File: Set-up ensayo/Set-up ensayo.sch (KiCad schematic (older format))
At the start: 14 parts, among them J1 Conn_Coaxial, J2 DB9_Female_MountingHoles

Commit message: Agregué al esquemático un potenciómetro variable y su footprint en paralelo a R de ensayo en caso de que necesite ser variada
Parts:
- added RV1: R_POT, Footprints proyecto:Potentiometer_Vishay_248GJ-249GJ_Single_Vertical, symbol Device:R_POT
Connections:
- net VZs1: now also RV1.2, RV1.3
- net Vi: now also RV1.1
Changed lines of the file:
@@
 Connection ~ 6900 4350
 Wire Wire Line
-	5400 3400 5200 3400
+	5400 3400 5300 3400
 Wire Wire Line
 	5700 3400 5950 3400
@@
 Text Label 2400 3500 0    50   ~ 0
 VAC
+$Comp
+L Device:R_POT RV1
+U 1 1 5D5409ED
+P 5550 3750
+F 0 "RV1" V 5435 3750 50  0000 C CNN
+F 1 "R_POT" V 5344 3750 50  0000 C CNN
+F 2 "Footprints proyecto:Potentiometer_Vishay_248GJ-249GJ_Single_Vertical" H 5550 3750 50  0001 C CNN
+F 3 "~" H 5550 3750 50  0001 C CNN
+F 4 "Resistencia auxiliar variable" V 5550 3750 50  0001 C CNN "Función"
+	1    5550 3750
+	0    -1   -1   0
+$EndComp
+Wire Wire Line
+	5300 3400 5300 3750
+Wire Wire Line
+	5300 3750 5400 3750
+Connection ~ 5300 3400
+Wire Wire Line
+	5300 3400 5200 3400
+Wire Wire Line
+	5550 3600 5950 3600
+Wire Wire Line
+	5950 3600 5950 3400
+Wire Wire Line
+	5700 3750 5950 3750
+Wire Wire Line
+	5950 3750 5950 3600
+Connection ~ 5950 3600
 $EndSCHEMATC

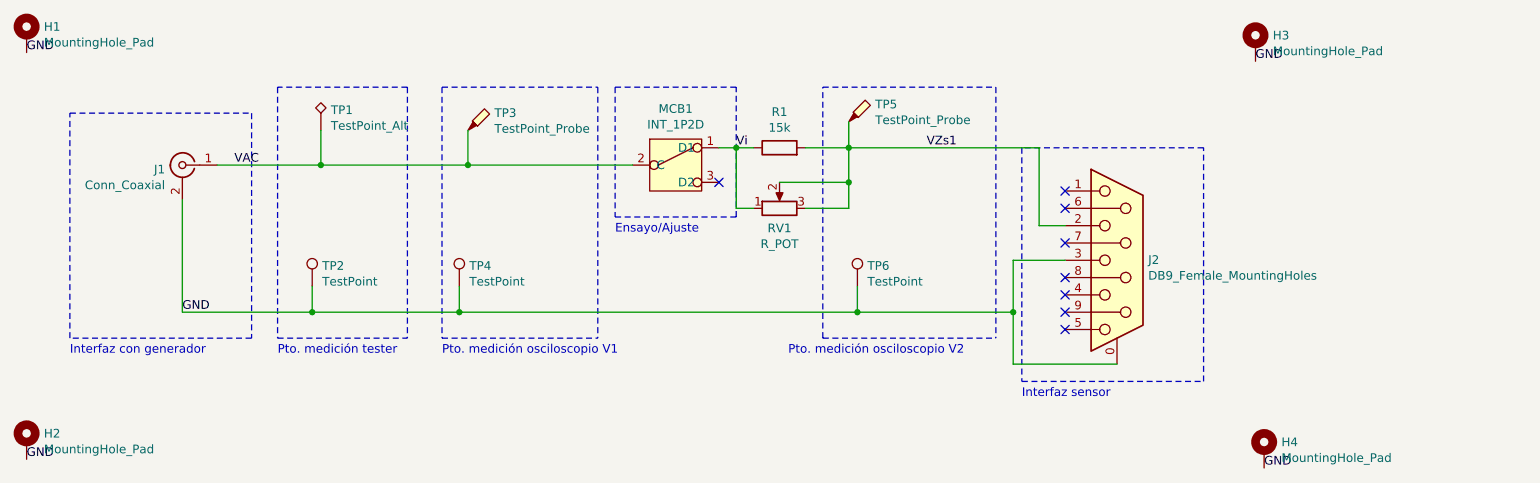
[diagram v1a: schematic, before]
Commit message: Agregué pines para configuración de resistencia variable o fija para ensayo
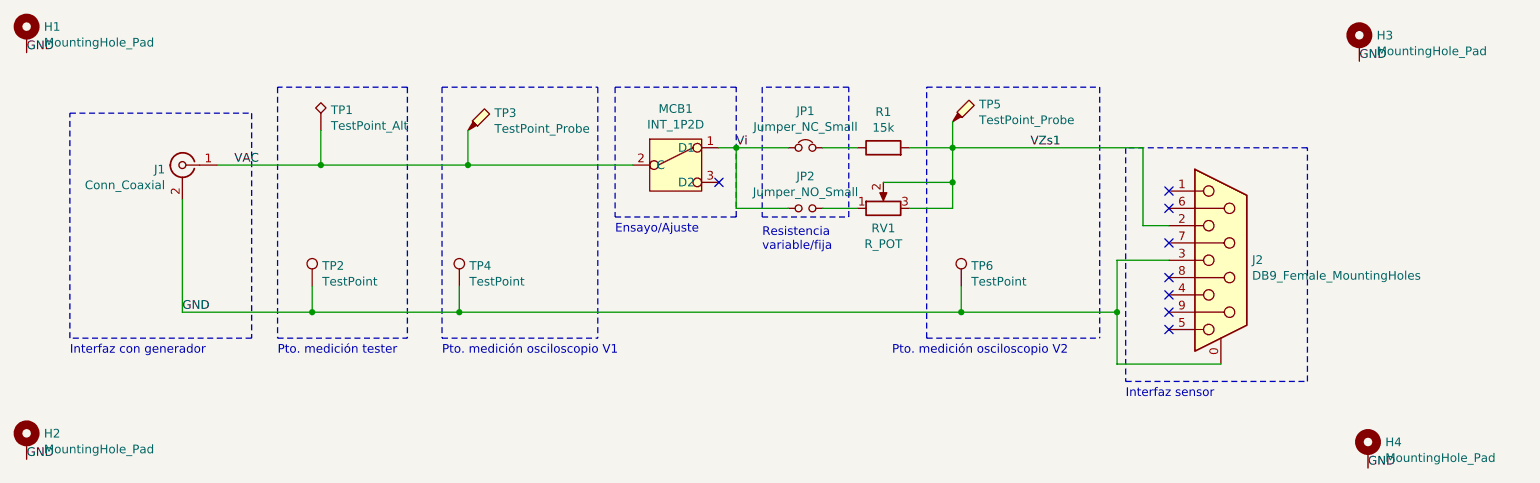
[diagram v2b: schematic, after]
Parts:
- added JP1: Jumper_NC_Small, Footprints proyecto:PinHeader_1x02_P1.00mm_Vertical, symbol Device:Jumper_NC_Small
- added JP2: Jumper_NO_Small, Footprints proyecto:PinHeader_1x02_P1.00mm_Vertical, symbol Device:Jumper_NO_Small
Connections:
- net Vi: now also JP1.1, JP2.1; no longer R1.1, RV1.1
- new net: JP1.2, R1.1
- new net: JP2.2, RV1.1
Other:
- note added: "Resistencia\nvariable/fija"
- moved on the sheet: H3, H4, J2, R1, RV1, TP5, TP6
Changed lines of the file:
@@
 L Mechanical:MountingHole_Pad H3
 U 1 1 5D42E2DA
-P 8300 2800
-F 0 "H3" H 8400 2849 50  0000 L CNN
-F 1 "MountingHole_Pad" H 8400 2758 50  0000 L CNN
-F 2 "Footprints proyecto:MountingHole_3.2mm_M3_ISO14580_Pad" H 8300 2800 50  0001 C CNN
-F 3 "~" H 8300 2800 50  0001 C CNN
-F 4 "Fijación e interfaz eléctrica con chasis" H 8300 2800 50  0001 C CNN "Función"
-	1    8300 2800
+P 8900 2800
+F 0 "H3" H 9000 2849 50  0000 L CNN
+F 1 "MountingHole_Pad" H 9000 2758 50  0000 L CNN
+F 2 "Footprints proyecto:MountingHole_3.2mm_M3_ISO14580_Pad" H 8900 2800 50  0001 C CNN
+F 3 "~" H 8900 2800 50  0001 C CNN
+F 4 "Fijación e interfaz eléctrica con chasis" H 8900 2800 50  0001 C CNN "Función"
+	1    8900 2800
 	1    0    0    -1
 $EndComp
@@
 L Mechanical:MountingHole_Pad H4
 U 1 1 5D42EA1B
-P 8350 5150
-F 0 "H4" H 8450 5199 50  0000 L CNN
-F 1 "MountingHole_Pad" H 8450 5108 50  0000 L CNN
-F 2 "Footprints proyecto:MountingHole_3.2mm_M3_ISO14580_Pad" H 8350 5150 50  0001 C CNN
-F 3 "~" H 8350 5150 50  0001 C CNN
-F 4 "Fijación e interfaz eléctrica con chasis" H 8350 5150 50  0001 C CNN "Función"
-	1    8350 5150
+P 8950 5150
+F 0 "H4" H 9050 5199 50  0000 L CNN
+F 1 "MountingHole_Pad" H 9050 5108 50  0000 L CNN
+F 2 "Footprints proyecto:MountingHole_3.2mm_M3_ISO14580_Pad" H 8950 5150 50  0001 C CNN
+F 3 "~" H 8950 5150 50  0001 C CNN
+F 4 "Fijación e interfaz eléctrica con chasis" H 8950 5150 50  0001 C CNN "Función"
+	1    8950 5150
 	1    0    0    -1
 $EndComp
@@
 L Device:R R1
 U 1 1 5D441970
-P 5550 3400
-F 0 "R1" V 5757 3400 50  0000 C CNN
-F 1 "15k" V 5666 3400 50  0000 C CNN
-F 2 "Footprints proyecto:R_Axial_DIN0204_L3.6mm_D1.6mm_P7.62mm_Horizontal" V 5480 3400 50  0001 C CNN
-F 3 "~" H 5550 3400 50  0001 C CNN
-F 4 "Resistencia de medición de sensor" V 5550 3400 50  0001 C CNN "Función"
-	1    5550 3400
+P 6150 3400
+F 0 "R1" V 6357 3400 50  0000 C CNN
+F 1 "15k" V 6266 3400 50  0000 C CNN
+F 2 "Footprints proyecto:R_Axial_DIN0204_L3.6mm_D1.6mm_P7.62mm_Horizontal" V 6080 3400 50  0001 C CNN
+F 3 "~" H 6150 3400 50  0001 C CNN
+F 4 "Resistencia de medición de sensor" V 6150 3400 50  0001 C CNN "Función"
+	1    6150 3400
 	0    -1   -1   0
 $EndComp
@@
 L Connector:DB9_Female_MountingHoles J2
 U 1 1 5D442DB3
-P 7500 4050
-F 0 "J2" H 7680 4052 50  0000 L CNN
-F 1 "DB9_Female_MountingHoles" H 7680 3961 50  0000 L CNN
-F 2 "Footprints proyecto:DSUB-9_Female_Horizontal_P2.77x2.84mm_EdgePinOffset4.94mm_Housed_MountingHolesOffset7.48mm" H 7500 4050 50  0001 C CNN
-F 3 " ~" H 7500 4050 50  0001 C CNN
-F 4 "Interfaz eléctrica con sensores" H 7500 4050 50  0001 C CNN "Función"
-	1    7500 4050
+P 8100 4050
+F 0 "J2" H 8280 4052 50  0000 L CNN
+F 1 "DB9_Female_MountingHoles" H 8280 3961 50  0000 L CNN
+F 2 "Footprints proyecto:DSUB-9_Female_Horizontal_P2.77x2.84mm_EdgePinOffset4.94mm_Housed_MountingHolesOffset7.48mm" H 8100 4050 50  0001 C CNN
+F 3 " ~" H 8100 4050 50  0001 C CNN
+F 4 "Interfaz eléctrica con sensores" H 8100 4050 50  0001 C CNN "Función"
+	1    8100 4050
 	1    0    0    -1
 $EndComp
@@
 L Connector:TestPoint_Probe TP5
 U 1 1 5D484196
-P 5950 3250
-F 0 "TP5" H 6103 3351 50  0000 L CNN
-F 1 "TestPoint_Probe" H 6103 3260 50  0000 L CNN
-F 2 "Footprints proyecto:PinHeader_1x01_P1.00mm_Horizontal" H 6150 3250 50  0001 C CNN
-F 3 "~" H 6150 3250 50  0001 C CNN
-F 4 "Interfaz eléctrica con punta de medición V2 osciloscopio" H 5950 3250 50  0001 C CNN "Función"
-	1    5950 3250
+P 6550 3250
+F 0 "TP5" H 6703 3351 50  0000 L CNN
+F 1 "TestPoint_Probe" H 6703 3260 50  0000 L CNN
+F 2 "Footprints proyecto:PinHeader_1x01_P1.00mm_Horizontal" H 6750 3250 50  0001 C CNN
+F 3 "~" H 6750 3250 50  0001 C CNN
+F 4 "Interfaz eléctrica con punta de medición V2 osciloscopio" H 6550 3250 50  0001 C CNN "Función"
+	1    6550 3250
 	1    0    0    -1
 $EndComp
@@
 L Connector:TestPoint TP6
 U 1 1 5D4852D2
-P 6000 4200
-F 0 "TP6" H 6058 4318 50  0000 L CNN
-F 1 "TestPoint" H 6058 4227 50  0000 L CNN
-F 2 "Footprints proyecto:PinHeader_1x01_P1.00mm_Horizontal" H 6200 4200 50  0001 C CNN
-F 3 "~" H 6200 4200 50  0001 C CNN
-F 4 "Interfaz eléctrica con GND de V2 osciloscopio" H 6000 4200 50  0001 C CNN "Función"
-	1    6000 4200
+P 6600 4200
+F 0 "TP6" H 6658 4318 50  0000 L CNN
+F 1 "TestPoint" H 6658 4227 50  0000 L CNN
+F 2 "Footprints proyecto:PinHeader_1x01_P1.00mm_Horizontal" H 6800 4200 50  0001 C CNN
+F 3 "~" H 6800 4200 50  0001 C CNN
+F 4 "Interfaz eléctrica con GND de V2 osciloscopio" H 6600 4200 50  0001 C CNN "Función"
+	1    6600 4200
 	1    0    0    -1
 $EndComp
@@
 Text Notes 4600 3900 0    50   ~ 0
 Ensayo/Ajuste
-Text Notes 5600 4600 0    50   ~ 0
+Text Notes 6200 4600 0    50   ~ 0
 Pto. medición osciloscopio V2
 Wire Notes Line
-	6950 3400 6950 4750
-Wire Notes Line
-	6950 4750 8000 4750
-Wire Notes Line
-	8000 4750 8000 3400
-Wire Notes Line
-	8000 3400 6950 3400
-Text Notes 6950 4850 0    50   ~ 0
+	7550 3400 7550 4750
+Wire Notes Line
+	7550 4750 8600 4750
+Wire Notes Line
+	8600 4750 8600 3400
+Wire Notes Line
+	8600 3400 7550 3400
+Text Notes 7550 4850 0    50   ~ 0
 Interfaz sensor
 Wire Wire Line
@@
 Connection ~ 2850 4350
 Wire Wire Line
-	6000 4350 6900 4350
-Wire Wire Line
-	6900 4350 6900 4650
-Wire Wire Line
-	6900 4650 7500 4650
-Connection ~ 6000 4350
-Wire Wire Line
-	7200 4050 6900 4050
-Wire Wire Line
-	6900 4050 6900 4350
-Connection ~ 6900 4350
-Wire Wire Line
-	5400 3400 5300 3400
-Wire Wire Line
-	5700 3400 5950 3400
-Wire Wire Line
-	7050 3400 7050 3850
-Wire Wire Line
-	7050 3850 7200 3850
+	6600 4350 7500 4350
+Wire Wire Line
+	7500 4350 7500 4650
+Wire Wire Line
+	7500 4650 8100 4650
+Connection ~ 6600 4350
+Wire Wire Line
+	7800 4050 7500 4050
+Wire Wire Line
+	7500 4050 7500 4350
+Connection ~ 7500 4350
+Wire Wire Line
+	6300 3400 6550 3400
+Wire Wire Line
+	7650 3400 7650 3850
+Wire Wire Line
+	7650 3850 7800 3850
 NoConn ~ 5200 3600
 Wire Wire Line
-	5950 3250 5950 3400
-Connection ~ 5950 3400
-Wire Wire Line
-	5950 3400 7050 3400
+	6550 3250 6550 3400
+Connection ~ 6550 3400
+Wire Wire Line
+	6550 3400 7650 3400
 Wire Wire Line
 	3700 4200 3700 4350
-Connection ~ 3700 4350
-Wire Wire Line
-	3700 4350 6000 4350
-Wire Notes Line
-	5800 4500 5800 3050
-Wire Notes Line
-	5800 3050 6800 3050
-Wire Notes Line
-	6800 3050 6800 4500
-Wire Notes Line
-	5800 4500 6800 4500
-Wire Wire Line
-	6000 4200 6000 4350
+Wire Notes Line
+	6400 4500 6400 3050
+Wire Notes Line
+	6400 3050 7400 3050
+Wire Notes Line
+	7400 3050 7400 4500
+Wire Notes Line
+	6400 4500 7400 4500
+Wire Wire Line
+	6600 4200 6600 4350
 Wire Notes Line
 	3600 3050 4500 3050
@@
 Text Label 2100 4350 0    50   ~ 0
 GND
-Text Label 6400 3400 0    50   ~ 0
+Text Label 7000 3400 0    50   ~ 0
 VZs1
 Text Label 1200 2850 0    50   ~ 0
@@
 Text Label 1200 5200 0    50   ~ 0
 GND
-Text Label 8350 5250 0    50   ~ 0
-GND
-Text Label 8300 2900 0    50   ~ 0
+Text Label 8950 5250 0    50   ~ 0
+GND
+Text Label 8900 2900 0    50   ~ 0
 GND
 Text Label 5300 3400 0    50   ~ 0
@@
 Wire Wire Line
 	2850 4200 2850 4350
-NoConn ~ 7200 3650
-NoConn ~ 7200 3750
-NoConn ~ 7200 3950
-NoConn ~ 7200 4150
-NoConn ~ 7200 4250
-NoConn ~ 7200 4350
-NoConn ~ 7200 4450
+NoConn ~ 7800 3650
+NoConn ~ 7800 3750
+NoConn ~ 7800 3950
+NoConn ~ 7800 4150
+NoConn ~ 7800 4250
+NoConn ~ 7800 4350
+NoConn ~ 7800 4450
 Wire Wire Line
 	2300 3500 2900 3500
@@
 L Device:R_POT RV1
 U 1 1 5D5409ED
-P 5550 3750
-F 0 "RV1" V 5435 3750 50  0000 C CNN
-F 1 "R_POT" V 5344 3750 50  0000 C CNN
-F 2 "Footprints proyecto:Potentiometer_Vishay_248GJ-249GJ_Single_Vertical" H 5550 3750 50  0001 C CNN
-F 3 "~" H 5550 3750 50  0001 C CNN
-F 4 "Resistencia auxiliar variable" V 5550 3750 50  0001 C CNN "Función"
-	1    5550 3750
+P 6150 3750
+F 0 "RV1" V 6035 3750 50  0000 C CNN
+F 1 "R_POT" V 5944 3750 50  0000 C CNN
+F 2 "Footprints proyecto:Potentiometer_Vishay_248GJ-249GJ_Single_Vertical" H 6150 3750 50  0001 C CNN
+F 3 "~" H 6150 3750 50  0001 C CNN
+F 4 "Resistencia auxiliar variable" V 6150 3750 50  0001 C CNN "Función"
+	1    6150 3750
 	0    -1   -1   0
 $EndComp
@@
 	5300 3400 5300 3750
 Wire Wire Line
-	5300 3750 5400 3750
+	6150 3600 6550 3600
+Wire Wire Line
+	6550 3600 6550 3400
+Wire Wire Line
+	6300 3750 6550 3750
+Wire Wire Line
+	6550 3750 6550 3600
+Connection ~ 6550 3600
+$Comp
+L Device:Jumper_NC_Small JP1
+U 1 1 5D552AB7
+P 5700 3400
+F 0 "JP1" H 5700 3612 50  0000 C CNN
+F 1 "Jumper_NC_Small" H 5700 3521 50  0000 C CNN
+F 2 "Footprints proyecto:PinHeader_1x02_P1.00mm_Vertical" H 5700 3400 50  0001 C CNN
+F 3 "~" H 5700 3400 50  0001 C CNN
+F 4 "Jumper para configuración de resistencia fija" H 5700 3400 50  0001 C CNN "Función"
+	1    5700 3400
+	1    0    0    -1
+$EndComp
+$Comp
+L Device:Jumper_NO_Small JP2
+U 1 1 5D55355E
+P 5700 3750
+F 0 "JP2" H 5700 3935 50  0000 C CNN
+F 1 "Jumper_NO_Small" H 5700 3844 50  0000 C CNN
+F 2 "Footprints proyecto:PinHeader_1x02_P1.00mm_Vertical" H 5700 3750 50  0001 C CNN
+F 3 "~" H 5700 3750 50  0001 C CNN
+F 4 "Jumper para configuración de resistencia variable" H 5700 3750 50  0001 C CNN "Función"
+	1    5700 3750
+	1    0    0    -1
+$EndComp
+Wire Wire Line
+	3700 4350 6600 4350
+Connection ~ 3700 4350
+Wire Wire Line
+	5200 3400 5300 3400
+Wire Wire Line
+	5800 3400 6000 3400
+Wire Wire Line
+	5300 3750 5600 3750
+Wire Wire Line
+	5800 3750 6000 3750
 Connection ~ 5300 3400
 Wire Wire Line
-	5300 3400 5200 3400
-Wire Wire Line
-	5550 3600 5950 3600
-Wire Wire Line
-	5950 3600 5950 3400
-Wire Wire Line
-	5700 3750 5950 3750
-Wire Wire Line
-	5950 3750 5950 3600
-Connection ~ 5950 3600
+	5300 3400 5600 3400
+Text Notes 5450 4000 0    50   ~ 0
+Resistencia\nvariable/fija
+Wire Notes Line
+	5450 3050 5450 3800
+Wire Notes Line
+	5450 3800 5950 3800
+Wire Notes Line
+	5950 3800 5950 3050
+Wire Notes Line
+	5950 3050 5450 3050
 $EndSCHEMATC
